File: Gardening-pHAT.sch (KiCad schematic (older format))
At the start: 20 parts, among them P1 CONN_01X03, P2 CONN_01X03, P3 CONN_01X03, P4 CONN_02X05, U1 CAT24C32WI-GT3, U2 MCP3002

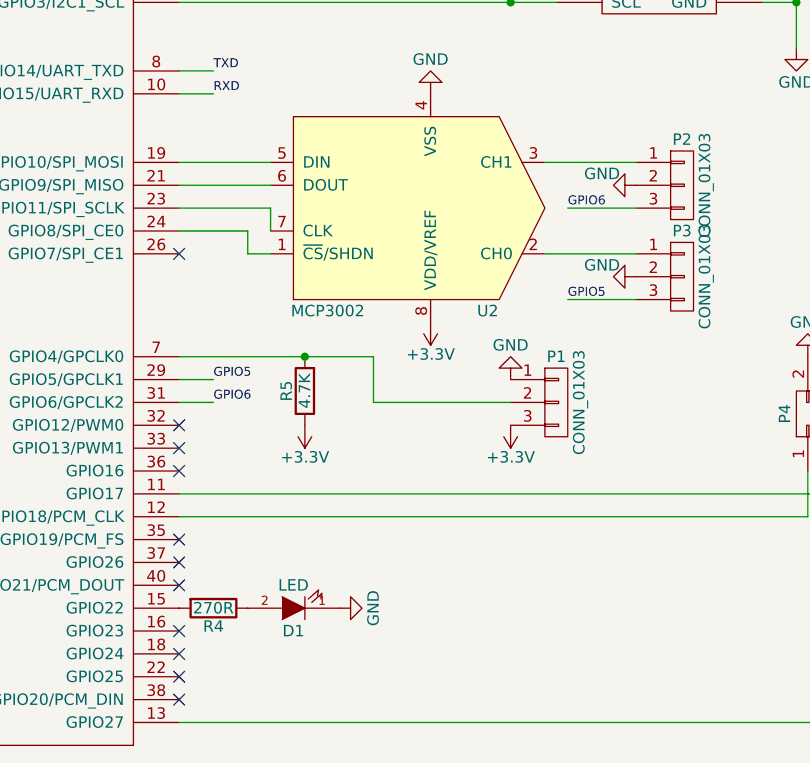
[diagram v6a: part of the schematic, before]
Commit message: Gardening-pHAT: Update tracks
Update tracks and labels.

Signed-off-by: Leon Anavi <leon@anavi.org>
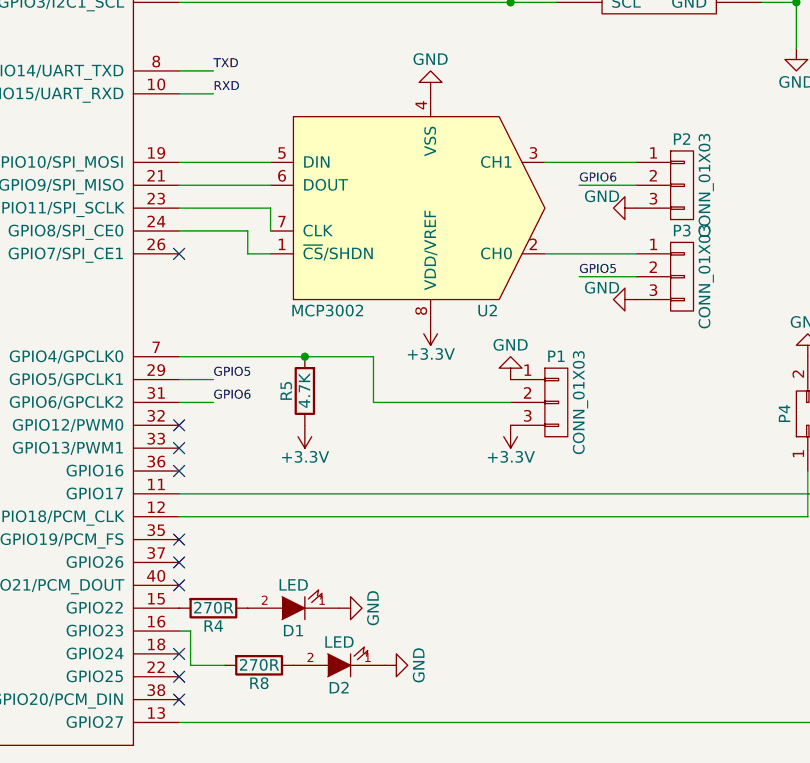
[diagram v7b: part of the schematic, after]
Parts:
- added D2: LED, LED_SMD:LED_1206_3216Metric, symbol Gardening-pHAT-rescue:LED
- added R8: 270R, Resistors_SMD:R_0603_HandSoldering, symbol Gardening-pHAT-rescue:R
- D1: footprint LEDs:LED-5MM -> LED_SMD:LED_1206_3216Metric
- P2, P3: footprint myfootprint:KLEMA_1x3 -> Pin_Headers:Pin_Header_Straight_1x03
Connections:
- net GND: now also P2.3 (P3), P3.3 (P3), D2.1 (K); no longer P2.2 (P2), P3.2 (P2)
- net GPIO5: now also P3.2 (P2); no longer P3.3 (P3)
- net GPIO6: now also P2.2 (P2); no longer P2.3 (P3)
- net at RASP_CONN1.16 (GPIO23): now also R8.2
- new net: D2.2 (A), R8.1
- no-connect marks 11 -> 10
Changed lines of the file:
@@
 NoConn ~ 5350 4850
 NoConn ~ 5350 4750
-NoConn ~ 5350 4650
 NoConn ~ 5350 4450
 NoConn ~ 5350 4350
@@
 F 0 "P2" H 7550 2900 50  0000 C CNN
 F 1 "CONN_01X03" V 7650 2700 50  0000 C CNN
-F 2 "myfootprint:KLEMA_1x3" H 7550 2700 50  0001 C CNN
+F 2 "Pin_Headers:Pin_Header_Straight_1x03" H 7550 2700 50  0001 C CNN
 F 3 "" H 7550 2700 50  0000 C CNN
 	1    7550 2700
@@
 F 0 "P3" H 7550 3300 50  0000 C CNN
 F 1 "CONN_01X03" V 7650 3100 50  0000 C CNN
-F 2 "myfootprint:KLEMA_1x3" H 7550 3100 50  0001 C CNN
+F 2 "Pin_Headers:Pin_Header_Straight_1x03" H 7550 3100 50  0001 C CNN
 F 3 "" H 7550 3100 50  0000 C CNN
 	1    7550 3100
@@
 F 0 "D1" H 5850 4650 50  0000 C CNN
 F 1 "LED" H 5850 4450 50  0000 C CNN
-F 2 "LEDs:LED-5MM" H 5850 4550 50  0001 C CNN
+F 2 "LED_SMD:LED_1206_3216Metric" H 5850 4550 50  0001 C CNN
 F 3 "" H 5850 4550 50  0000 C CNN
 	1    5850 4550
@@
 L Gardening-pHAT-rescue:GND #PWR025
 U 1 1 58F9E900
-P 7350 3100
-F 0 "#PWR025" H 7350 2850 50  0001 C CNN
-F 1 "GND" V 7300 2950 50  0000 C CNN
-F 2 "" H 7350 3100 50  0000 C CNN
-F 3 "" H 7350 3100 50  0000 C CNN
-	1    7350 3100
-	0    1    1    0
-$EndComp
-$Comp
-L Gardening-pHAT-rescue:GND #PWR026
-U 1 1 58F9E966
-P 7350 2700
-F 0 "#PWR026" H 7350 2450 50  0001 C CNN
-F 1 "GND" V 7300 2550 50  0000 C CNN
-F 2 "" H 7350 2700 50  0000 C CNN
-F 3 "" H 7350 2700 50  0000 C CNN
-	1    7350 2700
+P 7350 3200
+F 0 "#PWR025" H 7350 2950 50  0001 C CNN
+F 1 "GND" V 7300 3050 50  0000 C CNN
+F 2 "" H 7350 3200 50  0000 C CNN
+F 3 "" H 7350 3200 50  0000 C CNN
+	1    7350 3200
 	0    1    1    0
 $EndComp
@@
 Wire Wire Line
 	5500 3650 5350 3650
-Text Label 7050 3200 0    39   ~ 0
+Text Label 7100 3100 0    39   ~ 0
 GPIO5
 Wire Wire Line
-	7350 3200 7050 3200
-Text Label 7050 2800 0    39   ~ 0
+	800  3600 800  3700
+Wire Wire Line
+	800  3700 800  3800
+Wire Wire Line
+	800  3800 800  3950
+Wire Wire Line
+	2200 3050 2200 3500
+Wire Wire Line
+	2800 3050 2950 3050
+Wire Wire Line
+	2650 3050 2800 3050
+Wire Wire Line
+	2950 3800 3450 3800
+Wire Wire Line
+	2800 3700 3450 3700
+Wire Wire Line
+	2650 3600 2650 4050
+Wire Wire Line
+	6650 1800 7000 1800
+Wire Wire Line
+	6800 1900 7000 1900
+Wire Wire Line
+	8050 1900 8050 2100
+Wire Wire Line
+	6650 1200 7000 1200
+Wire Wire Line
+	6800 1300 7000 1300
+Wire Wire Line
+	6200 750  6350 750
+Wire Wire Line
+	3450 2750 3450 2850
+Wire Wire Line
+	3450 2850 3450 2950
+Wire Wire Line
+	3450 2950 3450 3050
+Wire Wire Line
+	3450 3050 3450 3150
+Wire Wire Line
+	3450 3150 3450 3250
+Wire Wire Line
+	3450 3350 3450 3450
+Wire Wire Line
+	3450 3250 3450 3350
+Wire Wire Line
+	5900 3450 6200 3450
+$Comp
+L Gardening-pHAT-rescue:LED D2
+U 1 1 609682D7
+P 6050 4800
+F 0 "D2" H 6050 4900 50  0000 C CNN
+F 1 "LED" H 6050 4700 50  0000 C CNN
+F 2 "LED_SMD:LED_1206_3216Metric" H 6050 4800 50  0001 C CNN
+F 3 "" H 6050 4800 50  0000 C CNN
+	1    6050 4800
+	-1   0    0    1
+$EndComp
+$Comp
+L Gardening-pHAT-rescue:R R8
+U 1 1 609682DD
+P 5700 4800
+F 0 "R8" V 5780 4800 50  0000 C CNN
+F 1 "270R" V 5700 4800 50  0000 C CNN
+F 2 "Resistors_SMD:R_0603_HandSoldering" V 5630 4800 50  0001 C CNN
+F 3 "" H 5700 4800 50  0000 C CNN
+	1    5700 4800
+	0    1    1    0
+$EndComp
+$Comp
+L Gardening-pHAT-rescue:GND #PWR0101
+U 1 1 609682E3
+P 6250 4800
+F 0 "#PWR0101" H 6250 4550 50  0001 C CNN
+F 1 "GND" H 6250 4650 50  0000 C CNN
+F 2 "" H 6250 4800 50  0000 C CNN
+F 3 "" H 6250 4800 50  0000 C CNN
+	1    6250 4800
+	0    -1   -1   0
+$EndComp
+Wire Wire Line
+	5350 4650 5400 4650
+Wire Wire Line
+	5400 4650 5400 4800
+Wire Wire Line
+	5400 4800 5550 4800
+Text Label 7100 2700 0    39   ~ 0
 GPIO6
-Wire Wire Line
-	7350 2800 7050 2800
-Wire Wire Line
-	800  3600 800  3700
-Wire Wire Line
-	800  3700 800  3800
-Wire Wire Line
-	800  3800 800  3950
-Wire Wire Line
-	2200 3050 2200 3500
-Wire Wire Line
-	2800 3050 2950 3050
-Wire Wire Line
-	2650 3050 2800 3050
-Wire Wire Line
-	2950 3800 3450 3800
-Wire Wire Line
-	2800 3700 3450 3700
-Wire Wire Line
-	2650 3600 2650 4050
-Wire Wire Line
-	6650 1800 7000 1800
-Wire Wire Line
-	6800 1900 7000 1900
-Wire Wire Line
-	8050 1900 8050 2100
-Wire Wire Line
-	6650 1200 7000 1200
-Wire Wire Line
-	6800 1300 7000 1300
-Wire Wire Line
-	6200 750  6350 750
-Wire Wire Line
-	3450 2750 3450 2850
-Wire Wire Line
-	3450 2850 3450 2950
-Wire Wire Line
-	3450 2950 3450 3050
-Wire Wire Line
-	3450 3050 3450 3150
-Wire Wire Line
-	3450 3150 3450 3250
-Wire Wire Line
-	3450 3350 3450 3450
-Wire Wire Line
-	3450 3250 3450 3350
-Wire Wire Line
-	5900 3450 6200 3450
+$Comp
+L Gardening-pHAT-rescue:GND #PWR026
+U 1 1 58F9E966
+P 7350 2800
+F 0 "#PWR026" H 7350 2550 50  0001 C CNN
+F 1 "GND" V 7300 2650 50  0000 C CNN
+F 2 "" H 7350 2800 50  0000 C CNN
+F 3 "" H 7350 2800 50  0000 C CNN
+	1    7350 2800
+	0    1    1    0
+$EndComp
+Wire Wire Line
+	7100 2700 7350 2700
+Wire Wire Line
+	7100 3100 7350 3100
 $EndSCHEMATC

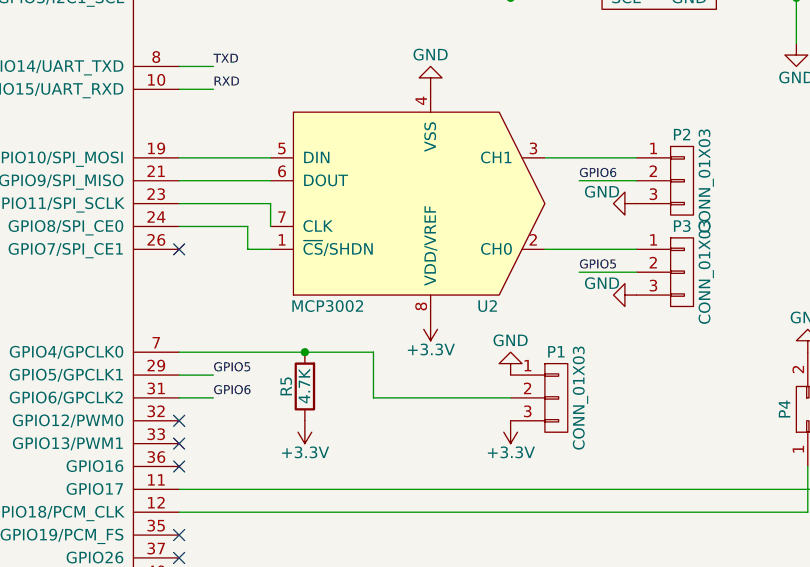
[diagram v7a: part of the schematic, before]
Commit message: Add fabrication labels for assemly
Create additional labels on the fabrication layer to help with
the SMT assembly of the PCB.

Signed-off-by: Leon Anavi <leon@anavi.org>
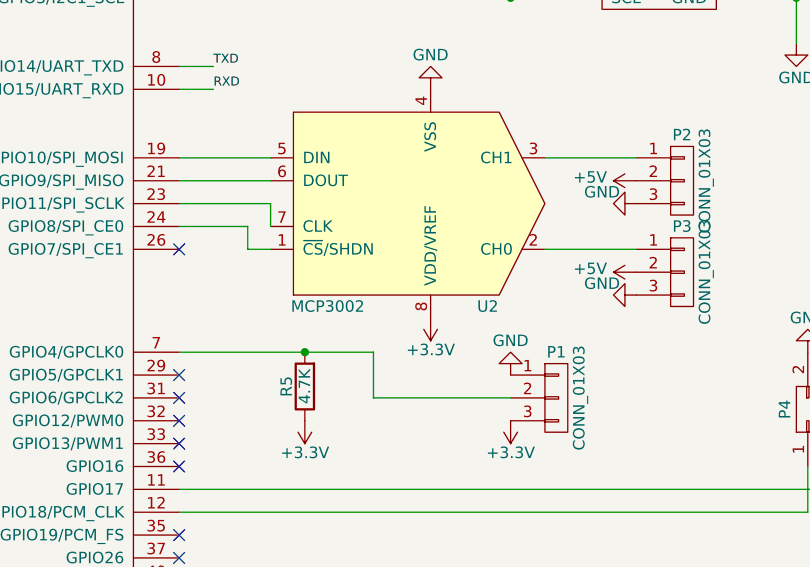
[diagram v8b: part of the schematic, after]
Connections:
- net +5V: now also P2.2 (P2), P3.2 (P2)
- net GPIO5: no longer names the net of RASP_CONN1.29 (GPIO5/GPCLK1)
- net GPIO5: no longer P3.2 (P2)
- net GPIO6: no longer names the net of RASP_CONN1.31 (GPIO6/GPCLK2)
- net GPIO6: no longer P2.2 (P2)
- no-connect marks 10 -> 12
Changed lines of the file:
@@
 	-1   0    0    1
 $EndComp
-Text Label 5500 3550 0    39   ~ 0
-GPIO5
-Text Label 5500 3650 0    39   ~ 0
-GPIO6
 Wire Wire Line
 	950  3500 800  3500
@@
 	6200 3650 6800 3650
 Connection ~ 5900 3450
-Wire Wire Line
-	5500 3550 5350 3550
-Wire Wire Line
-	5500 3650 5350 3650
-Text Label 7100 3100 0    39   ~ 0
-GPIO5
 Wire Wire Line
 	800  3600 800  3700
@@
 Wire Wire Line
 	5400 4800 5550 4800
-Text Label 7100 2700 0    39   ~ 0
-GPIO6
 $Comp
 L Gardening-pHAT-rescue:GND #PWR026
@@
 	0    1    1    0
 $EndComp
-Wire Wire Line
-	7100 2700 7350 2700
-Wire Wire Line
-	7100 3100 7350 3100
+NoConn ~ 5350 3550
+NoConn ~ 5350 3650
+$Comp
+L Gardening-pHAT-rescue:+5V #PWR0102
+U 1 1 60BA6F51
+P 7350 2700
+F 0 "#PWR0102" H 7350 2550 50  0001 C CNN
+F 1 "+5V" V 7365 2828 50  0000 L CNN
+F 2 "" H 7350 2700 50  0000 C CNN
+F 3 "" H 7350 2700 50  0000 C CNN
+	1    7350 2700
+	0    -1   -1   0
+$EndComp
+$Comp
+L Gardening-pHAT-rescue:+5V #PWR0103
+U 1 1 60BAC5CE
+P 7350 3100
+F 0 "#PWR0103" H 7350 2950 50  0001 C CNN
+F 1 "+5V" V 7365 3228 50  0000 L CNN
+F 2 "" H 7350 3100 50  0000 C CNN
+F 3 "" H 7350 3100 50  0000 C CNN
+	1    7350 3100
+	0    -1   -1   0
+$EndComp
 $EndSCHEMATC
